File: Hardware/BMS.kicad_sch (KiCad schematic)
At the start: 24 parts, among them J1 vcc, J2 gnd, U4 BQ51050BRHL

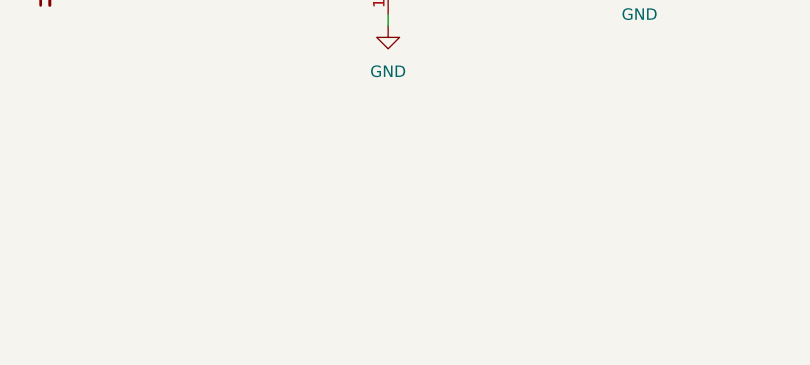
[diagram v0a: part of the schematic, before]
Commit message: add 100k external pull-up resistor to BMS Status line
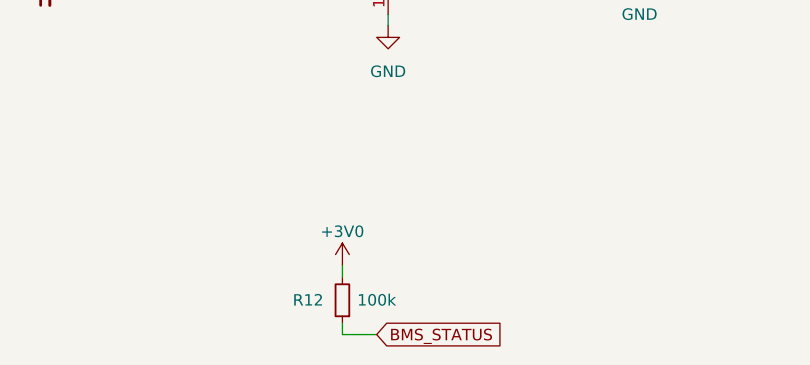
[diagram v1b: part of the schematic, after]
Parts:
- added R12: 100k, Resistor_SMD:R_0402_1005Metric, symbol Device:R_Small
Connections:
- net BMS_STATUS: now also R12.1
- new net +3V0: R12.2
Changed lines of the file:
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@@
+	(wire
+		(pts
+			(xy 135.89 107.95) (xy 135.89 106.68)
+		)
+		(stroke
+			(width 0)
+			(type default)
+		)
+	)
 	(wire
 		(pts
@@
 	(wire
 		(pts
+			(xy 139.7 107.95) (xy 135.89 107.95)
+		)
+		(stroke
+			(width 0)
+			(type default)
+		)
+	)
+	(wire
+		(pts
 			(xy 167.64 44.45) (xy 166.37 44.45)
 		)
@@
 		(pts
 			(xy 153.67 62.23) (xy 168.91 62.23)
+		)
+		(stroke
+			(width 0)
+			(type default)
+		)
+	)
+	(wire
+		(pts
+			(xy 135.89 101.6) (xy 135.89 100.33)
 		)
 		(stroke
@@
 		(property "Intersheetrefs" "${INTERSHEET_REFS}"
 			(at 169.597 34.29 0)
+			(effects
+				(font
+					(size 1.27 1.27)
+				)
+				(justify left)
+				(hide yes)
+			)
+		)
+	)
+	(global_label "BMS_STATUS"
+		(shape input)
+		(at 139.7 107.95 0)
+		(fields_autoplaced yes)
+		(effects
+			(font
+				(size 1.27 1.27)
+			)
+			(justify left)
+		)
+		(property "Intersheetrefs" "${INTERSHEET_REFS}"
+			(at 154.357 107.95 0)
 			(effects
 				(font
@@
 				(path "/fa78ac01-f44d-4d2a-889a-213ee2d7711c/48b428d0-0ac5-4ff0-aa96-29f30747e1b3"
 					(reference "C16")
+					(unit 1)
+				)
+			)
+		)
+	)
+	(symbol
+		(lib_id "power:+3V0")
+		(at 135.89 100.33 0)
+		(mirror y)
+		(unit 1)
+		(exclude_from_sim no)
+		(in_bom yes)
+		(on_board yes)
+		(dnp no)
+		(property "Reference" "#PWR054"
+			(at 135.89 104.14 0)
+			(effects
+				(font
+					(size 1.27 1.27)
+				)
+				(hide yes)
+			)
+		)
+		(property "Value" "+3V0"
+			(at 135.89 96.52 0)
+			(effects
+				(font
+					(size 1.27 1.27)
+				)
+			)
+		)
+		(property "Footprint" ""
+			(at 135.89 100.33 0)
+			(effects
+				(font
+					(size 1.27 1.27)
+				)
+				(hide yes)
+			)
+		)
+		(property "Datasheet" ""
+			(at 135.89 100.33 0)
+			(effects
+				(font
+					(size 1.27 1.27)
+				)
+				(hide yes)
+			)
+		)
+		(property "Description" "Power symbol creates a global label with name \"+3V0\""
+			(at 135.89 100.33 0)
+			(effects
+				(font
+					(size 1.27 1.27)
+				)
+				(hide yes)
+			)
+		)
+		(pin "1"
+		)
+		(instances
+			(project "WristWatch"
+				(path "/fa78ac01-f44d-4d2a-889a-213ee2d7711c/48b428d0-0ac5-4ff0-aa96-29f30747e1b3"
+					(reference "#PWR054")
 					(unit 1)
 				)
@@
 					(unit 1)
 				)
+			)
+		)
+	)
+	(symbol
+		(lib_id "Device:R_Small")
+		(at 135.89 104.14 180)
+		(unit 1)
+		(exclude_from_sim no)
+		(in_bom yes)
+		(on_board yes)
+		(dnp no)
+		(property "Reference" "R12"
+			(at 132.08 104.14 0)
+			(effects
+				(font
+					(size 1.27 1.27)
+				)
+			)
+		)
+		(property "Value" "100k"
+			(at 139.7 104.14 0)
+			(effects
+				(font
+					(size 1.27 1.27)
+				)
+			)
+		)
+		(property "Footprint" "Resistor_SMD:R_0402_1005Metric"
+			(at 135.89 104.14 0)
+			(effects
+				(font
+					(size 1.27 1.27)
+				)
+				(hide yes)
+			)
+		)
+		(property "Datasheet" "~"
+			(at 135.89 104.14 0)
+			(effects
+				(font
+					(size 1.27 1.27)
+				)
+				(hide yes)
+			)
+		)
+		(property "Description" "Resistor, small symbol"
+			(at 135.89 104.14 0)
+			(effects
+				(font
+					(size 1.27 1.27)
+				)
+				(hide yes)
+			)
+		)
+		(pin "2"
+		)
+		(pin "1"
+		)
+		(instances
+			(project "WristWatch"
+				(path "/fa78ac01-f44d-4d2a-889a-213ee2d7711c/48b428d0-0ac5-4ff0-aa96-29f30747e1b3"
+					(reference "R12")
+					(unit 1)
+				)
